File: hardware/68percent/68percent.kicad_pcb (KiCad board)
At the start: 4 copper layers, 123.8 x 142.9 mm, 119 parts, among them IC1 LD1117-3.3V-SOT223, J1 Conn_01x06, SW1 ROT_SKYLOONG_HS, SW2 Push_Button, Y1 8MHz

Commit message: pcb
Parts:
- removed LED1, LED10, LED11, LED12, LED13, LED14, LED15, LED16, LED17, LED18, LED19, LED2, LED20, LED21, LED22, LED23, LED24, LED25, LED26, LED27, LED3, LED4, LED5, LED6, LED7, LED8, LED9: MX_SK6812MINI-E, PCM_marbastlib-mx:LED_MX_6028R
- removed MACRO_A1, MACRO_B1, MACRO_C1, MACRO_D1, MACRO_E1, MACRO_F1, MACRO_G1, MACRO_H1, MACRO_I1, NUM_0, NUM_1, NUM_10, NUM_2, NUM_3, NUM_4, NUM_5, NUM_6, NUM_7, NUM_8, NUM_ADD1, NUM_DIV1, NUM_ENTER1, NUM_LOCK1, NUM_MULT1, NUM_PERIOD1, NUM_SUB1: MX_SW_HS, PCM_marbastlib-mx:SW_MX_HS_CPG151101S11_1u
- removed S1, S2, S3: MX_stab, PCM_marbastlib-mx:STAB_MX_P_2u
- removed SW1: ROT_SKYLOONG_HS, PCM_marbastlib-various:ROT_SKYLOONG_HS-Switch
- added D30: 1N4148W, PCM_Diode_SMD_AKL:D_SOD-123, B.Cu at (-145.3, 39.7)
- added D31: 1N4148W, PCM_Diode_SMD_AKL:D_SOD-123, B.Cu at (-145.3, 43.8)
- added D32: 1N4148W, PCM_Diode_SMD_AKL:D_SOD-123, B.Cu at (-145.3, 47.9)
- added D33: 1N4148W, PCM_Diode_SMD_AKL:D_SOD-123, B.Cu at (-151.3, 11.0)
- added D34: 1N4148W, PCM_Diode_SMD_AKL:D_SOD-123, B.Cu at (-151.3, 15.1)
- added D35: 1N4148W, PCM_Diode_SMD_AKL:D_SOD-123, B.Cu at (-151.3, 19.2)
- added D36: 1N4148W, PCM_Diode_SMD_AKL:D_SOD-123, B.Cu at (-151.3, 23.3)
- added D37: 1N4148W, PCM_Diode_SMD_AKL:D_SOD-123, B.Cu at (-151.3, 27.4)
- added D38: 1N4148W, PCM_Diode_SMD_AKL:D_SOD-123, B.Cu at (-151.3, 31.5)
- added D39: 1N4148W, PCM_Diode_SMD_AKL:D_SOD-123, B.Cu at (-151.3, 35.6)
- added D40: 1N4148W, PCM_Diode_SMD_AKL:D_SOD-123, B.Cu at (-151.3, 39.7)
- added D41: 1N4148W, PCM_Diode_SMD_AKL:D_SOD-123, B.Cu at (-151.3, 43.8)
- added D42: 1N4148W, PCM_Diode_SMD_AKL:D_SOD-123, B.Cu at (-151.3, 47.9)
- added D43: 1N4148W, PCM_Diode_SMD_AKL:D_SOD-123, B.Cu at (-157.2, 11.0)
- added D44: 1N4148W, PCM_Diode_SMD_AKL:D_SOD-123, B.Cu at (-157.2, 15.1)
- added D45: 1N4148W, PCM_Diode_SMD_AKL:D_SOD-123, B.Cu at (-157.2, 19.2)
- added D46: 1N4148W, PCM_Diode_SMD_AKL:D_SOD-123, B.Cu at (-157.2, 23.3)
- added D47: 1N4148W, PCM_Diode_SMD_AKL:D_SOD-123, B.Cu at (-157.2, 27.4)
- added D48: 1N4148W, PCM_Diode_SMD_AKL:D_SOD-123, B.Cu at (-157.2, 31.5)
- added D50: 1N4148W, PCM_Diode_SMD_AKL:D_SOD-123, B.Cu at (-157.2, 35.6)
- added D51: 1N4148W, PCM_Diode_SMD_AKL:D_SOD-123, B.Cu at (-157.2, 39.7)
- added D52: 1N4148W, PCM_Diode_SMD_AKL:D_SOD-123, B.Cu at (-157.2, 43.8)
- added D53: 1N4148W, PCM_Diode_SMD_AKL:D_SOD-123, B.Cu at (-157.2, 47.9)
- added D54: 1N4148W, PCM_Diode_SMD_AKL:D_SOD-123, B.Cu at (-163.1, 11.0)
- added D55: 1N4148W, PCM_Diode_SMD_AKL:D_SOD-123, B.Cu at (-163.1, 15.1)
- added D56: 1N4148W, PCM_Diode_SMD_AKL:D_SOD-123, B.Cu at (-163.1, 19.2)
- added D57: 1N4148W, PCM_Diode_SMD_AKL:D_SOD-123, B.Cu at (-163.1, 23.3)
- added D58: 1N4148W, PCM_Diode_SMD_AKL:D_SOD-123, B.Cu at (-163.1, 27.4)
- added D59: 1N4148W, PCM_Diode_SMD_AKL:D_SOD-123, B.Cu at (-163.1, 31.5)
- added D60: 1N4148W, PCM_Diode_SMD_AKL:D_SOD-123, B.Cu at (-163.1, 35.6)
- added D61: 1N4148W, PCM_Diode_SMD_AKL:D_SOD-123, B.Cu at (-163.1, 39.7)
- added D62: 1N4148W, PCM_Diode_SMD_AKL:D_SOD-123, B.Cu at (-163.1, 43.8)
- added D64: 1N4148W, PCM_Diode_SMD_AKL:D_SOD-123, B.Cu at (-163.1, 47.9)
- added D65: 1N4148W, PCM_Diode_SMD_AKL:D_SOD-123, B.Cu at (-169.0, 11.0)
- added D68: 1N4148W, PCM_Diode_SMD_AKL:D_SOD-123, B.Cu at (-169.0, 15.1)
- added D71: 1N4148W, PCM_Diode_SMD_AKL:D_SOD-123, B.Cu at (-169.0, 19.2)
- added D72: 1N4148W, PCM_Diode_SMD_AKL:D_SOD-123, B.Cu at (-169.0, 23.3)
- added D73: 1N4148W, PCM_Diode_SMD_AKL:D_SOD-123, B.Cu at (-169.0, 27.4)
- added D74: 1N4148W, PCM_Diode_SMD_AKL:D_SOD-123, B.Cu at (-169.0, 31.5)
- added D75: 1N4148W, PCM_Diode_SMD_AKL:D_SOD-123, B.Cu at (-169.0, 35.6)
- added D76: 1N4148W, PCM_Diode_SMD_AKL:D_SOD-123, B.Cu at (-169.0, 39.7)
- added KEY_'1: MX_SW_HS, PCM_marbastlib-mx:SW_MX_HS_CPG151101S11_1u, B.Cu at (-35.6, 16.5)
- added KEY_,1: MX_SW_HS, PCM_marbastlib-mx:SW_MX_HS_CPG151101S11_1u, B.Cu at (-35.6, 31.5)
- added KEY_.1: MX_SW_HS, PCM_marbastlib-mx:SW_MX_HS_CPG151101S11_1u, B.Cu at (-35.6, 46.6)
- added KEY_/1: MX_SW_HS, PCM_marbastlib-mx:SW_MX_HS_CPG151101S11_1u, B.Cu at (-35.6, 61.6)
- added KEY_0: MX_SW_HS, PCM_marbastlib-mx:SW_MX_HS_CPG151101S11_1u, B.Cu at (-18.4, 16.5)
- added KEY_1: MX_SW_HS, PCM_marbastlib-mx:SW_MX_HS_CPG151101S11_1u, B.Cu at (-18.4, 31.5)
- added KEY_2: MX_SW_HS, PCM_marbastlib-mx:SW_MX_HS_CPG151101S11_1u, B.Cu at (-18.4, 46.6)
- added KEY_3: MX_SW_HS, PCM_marbastlib-mx:SW_MX_HS_CPG151101S11_1u, B.Cu at (-18.4, 61.6)
- added KEY_4: MX_SW_HS, PCM_marbastlib-mx:SW_MX_HS_CPG151101S11_1u, B.Cu at (-18.4, 76.7)
- added KEY_5: MX_SW_HS, PCM_marbastlib-mx:SW_MX_HS_CPG151101S11_1u, B.Cu at (-18.4, 91.7)
- added KEY_6: MX_SW_HS, PCM_marbastlib-mx:SW_MX_HS_CPG151101S11_1u, B.Cu at (-18.4, 106.8)
- added KEY_7: MX_SW_HS, PCM_marbastlib-mx:SW_MX_HS_CPG151101S11_1u, B.Cu at (-18.4, 121.8)
- added KEY_8: MX_SW_HS, PCM_marbastlib-mx:SW_MX_HS_CPG151101S11_1u, B.Cu at (-18.4, 136.9)
- added KEY_9: MX_SW_HS, PCM_marbastlib-mx:SW_MX_HS_CPG151101S11_1u, B.Cu at (-18.4, 151.9)
- added KEY_;1: MX_SW_HS, PCM_marbastlib-mx:SW_MX_HS_CPG151101S11_1u, B.Cu at (-35.6, 76.7)
- added KEY_A1: MX_SW_HS, PCM_marbastlib-mx:SW_MX_HS_CPG151101S11_1u, B.Cu at (-35.6, 91.7)
- added KEY_ALT1: MX_SW_HS, PCM_marbastlib-mx:SW_MX_HS_CPG151101S11_1u, B.Cu at (-35.6, 106.8)
- added KEY_ALT2: MX_SW_HS, PCM_marbastlib-mx:SW_MX_HS_CPG151101S11_1u, B.Cu at (-35.6, 121.8)
- added KEY_B1: MX_SW_HS, PCM_marbastlib-mx:SW_MX_HS_CPG151101S11_1u, B.Cu at (-35.6, 136.9)
- added KEY_BKSP1: MX_SW_HS, PCM_marbastlib-mx:SW_MX_HS_CPG151101S11_1u, B.Cu at (-35.6, 151.9)
- added KEY_C1: MX_SW_HS, PCM_marbastlib-mx:SW_MX_HS_CPG151101S11_1u, B.Cu at (-52.7, 16.5)
- added KEY_CAPS1: MX_SW_HS, PCM_marbastlib-mx:SW_MX_HS_CPG151101S11_1u, B.Cu at (-52.7, 31.5)
- added KEY_CTRL1: MX_SW_HS, PCM_marbastlib-mx:SW_MX_HS_CPG151101S11_1u, B.Cu at (-52.7, 46.6)
- added KEY_CTRL2: MX_SW_HS, PCM_marbastlib-mx:SW_MX_HS_CPG151101S11_1u, B.Cu at (-52.7, 61.6)
- added KEY_D1: MX_SW_HS, PCM_marbastlib-mx:SW_MX_HS_CPG151101S11_1u, B.Cu at (-52.7, 76.7)
- added KEY_DARROW1: MX_SW_HS, PCM_marbastlib-mx:SW_MX_HS_CPG151101S11_1u, B.Cu at (-52.7, 91.7)
- added KEY_DARROW2: MX_SW_HS, PCM_marbastlib-mx:SW_MX_HS_CPG151101S11_1u, B.Cu at (-52.7, 106.8)
- added KEY_DEL1: MX_SW_HS, PCM_marbastlib-mx:SW_MX_HS_CPG151101S11_1u, B.Cu at (-52.7, 121.8)
- added KEY_E1: MX_SW_HS, PCM_marbastlib-mx:SW_MX_HS_CPG151101S11_1u, B.Cu at (-52.7, 136.9)
- added KEY_ENTER1: MX_SW_HS, PCM_marbastlib-mx:SW_MX_HS_CPG151101S11_1u, B.Cu at (-52.7, 151.9)
- added KEY_ESC1: MX_SW_HS, PCM_marbastlib-mx:SW_MX_HS_CPG151101S11_1u, B.Cu at (-69.9, 16.5)
- added KEY_F1: MX_SW_HS, PCM_marbastlib-mx:SW_MX_HS_CPG151101S11_1u, B.Cu at (-69.9, 31.5)
- added KEY_FN1: MX_SW_HS, PCM_marbastlib-mx:SW_MX_HS_CPG151101S11_1u, B.Cu at (-69.9, 46.6)
- added KEY_G1: MX_SW_HS, PCM_marbastlib-mx:SW_MX_HS_CPG151101S11_1u, B.Cu at (-69.9, 61.6)
- added KEY_H1: MX_SW_HS, PCM_marbastlib-mx:SW_MX_HS_CPG151101S11_1u, B.Cu at (-69.9, 76.7)
- added KEY_HOME1: MX_SW_HS, PCM_marbastlib-mx:SW_MX_HS_CPG151101S11_1u, B.Cu at (-69.9, 91.7)
- added KEY_I1: MX_SW_HS, PCM_marbastlib-mx:SW_MX_HS_CPG151101S11_1u, B.Cu at (-69.9, 106.8)
- added KEY_J1: MX_SW_HS, PCM_marbastlib-mx:SW_MX_HS_CPG151101S11_1u, B.Cu at (-69.9, 121.8)
- added KEY_K1: MX_SW_HS, PCM_marbastlib-mx:SW_MX_HS_CPG151101S11_1u, B.Cu at (-69.9, 136.9)
- added KEY_L1: MX_SW_HS, PCM_marbastlib-mx:SW_MX_HS_CPG151101S11_1u, B.Cu at (-69.9, 151.9)
- added KEY_M1: MX_SW_HS, PCM_marbastlib-mx:SW_MX_HS_CPG151101S11_1u, B.Cu at (-87.0, 16.5)
- added KEY_MINUS1: MX_SW_HS, PCM_marbastlib-mx:SW_MX_HS_CPG151101S11_1u, B.Cu at (-87.0, 31.5)
- added KEY_N1: MX_SW_HS, PCM_marbastlib-mx:SW_MX_HS_CPG151101S11_1u, B.Cu at (-87.0, 46.6)
- added KEY_O1: MX_SW_HS, PCM_marbastlib-mx:SW_MX_HS_CPG151101S11_1u, B.Cu at (-87.0, 61.6)
- added KEY_P1: MX_SW_HS, PCM_marbastlib-mx:SW_MX_HS_CPG151101S11_1u, B.Cu at (-87.0, 76.7)
- added KEY_PGDN1: MX_SW_HS, PCM_marbastlib-mx:SW_MX_HS_CPG151101S11_1u, B.Cu at (-87.0, 91.7)
- added KEY_PGUP1: MX_SW_HS, PCM_marbastlib-mx:SW_MX_HS_CPG151101S11_1u, B.Cu at (-87.0, 106.8)
- added KEY_PLUS1: MX_SW_HS, PCM_marbastlib-mx:SW_MX_HS_CPG151101S11_1u, B.Cu at (-87.0, 121.8)
- added KEY_Q1: MX_SW_HS, PCM_marbastlib-mx:SW_MX_HS_CPG151101S11_1u, B.Cu at (-87.0, 136.9)
- added KEY_R1: MX_SW_HS, PCM_marbastlib-mx:SW_MX_HS_CPG151101S11_1u, B.Cu at (-87.0, 151.9)
- added KEY_RARROW1: MX_SW_HS, PCM_marbastlib-mx:SW_MX_HS_CPG151101S11_1u, B.Cu at (-104.2, 16.5)
- added KEY_S1: MX_SW_HS, PCM_marbastlib-mx:SW_MX_HS_CPG151101S11_1u, B.Cu at (-104.2, 31.5)
- added KEY_SHIFT1: MX_SW_HS, PCM_marbastlib-mx:SW_MX_HS_CPG151101S11_1u, B.Cu at (-104.2, 46.6)
- added KEY_SHIFT2: MX_SW_HS, PCM_marbastlib-mx:SW_MX_HS_CPG151101S11_1u, B.Cu at (-104.2, 61.6)
- added KEY_SPACE1: MX_SW_HS, PCM_marbastlib-mx:SW_MX_HS_CPG151101S11_1u, B.Cu at (-104.2, 76.7)
- added KEY_T1: MX_SW_HS, PCM_marbastlib-mx:SW_MX_HS_CPG151101S11_1u, B.Cu at (-104.2, 91.7)
- added KEY_TAB1: MX_SW_HS, PCM_marbastlib-mx:SW_MX_HS_CPG151101S11_1u, B.Cu at (-104.2, 106.8)
- added KEY_U1: MX_SW_HS, PCM_marbastlib-mx:SW_MX_HS_CPG151101S11_1u, B.Cu at (-104.2, 121.8)
- added KEY_UARROW1: MX_SW_HS, PCM_marbastlib-mx:SW_MX_HS_CPG151101S11_1u, B.Cu at (-104.2, 136.9)
- added KEY_V1: MX_SW_HS, PCM_marbastlib-mx:SW_MX_HS_CPG151101S11_1u, B.Cu at (-104.2, 151.9)
- added KEY_W1: MX_SW_HS, PCM_marbastlib-mx:SW_MX_HS_CPG151101S11_1u, B.Cu at (-121.3, 16.5)
- added KEY_WIN1: MX_SW_HS, PCM_marbastlib-mx:SW_MX_HS_CPG151101S11_1u, B.Cu at (-121.3, 31.5)
- added KEY_X1: MX_SW_HS, PCM_marbastlib-mx:SW_MX_HS_CPG151101S11_1u, B.Cu at (-121.3, 46.6)
- added KEY_Y1: MX_SW_HS, PCM_marbastlib-mx:SW_MX_HS_CPG151101S11_1u, B.Cu at (-121.3, 61.6)
- added KEY_Z1: MX_SW_HS, PCM_marbastlib-mx:SW_MX_HS_CPG151101S11_1u, B.Cu at (-121.3, 76.7)
- added KEY_[1: MX_SW_HS, PCM_marbastlib-mx:SW_MX_HS_CPG151101S11_1u, B.Cu at (-121.3, 91.7)
- added KEY_\1: MX_SW_HS, PCM_marbastlib-mx:SW_MX_HS_CPG151101S11_1u, B.Cu at (-121.3, 106.8)
- added KEY_]1: MX_SW_HS, PCM_marbastlib-mx:SW_MX_HS_CPG151101S11_1u, B.Cu at (-121.3, 121.8)
- East1, North1, South1: moved to B.Cu
- moved D23 309.7 mm to (-145.3, 11.0)
- moved D21 288.8 mm to (-139.4, 43.8), turned to 180 degrees
- moved D14 283.1 mm to (-139.4, 15.1), turned to 180 degrees
- moved D20 281.8 mm to (-139.4, 39.7)
- moved D17 279.0 mm to (-139.4, 27.4)
- moved D13 278.0 mm to (-139.4, 11.0)
- moved D6 273.5 mm to (-133.5, 23.3)
- moved D19 266.2 mm to (-139.4, 35.6)
- moved D10 265.9 mm to (-133.5, 39.7), turned to 180 degrees
- moved D9 265.8 mm to (-133.5, 35.6)
- moved D16 263.4 mm to (-139.4, 23.3)
- moved D22 261.3 mm to (-139.4, 47.9)
- moved D5 255.5 mm to (-133.5, 19.2)
- moved D18 251.1 mm to (-139.4, 31.5)
- moved D8 248.4 mm to (-133.5, 31.5)
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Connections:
- D10 pad 1: /ROW2 -> /ROW1
- D11 pad 1: /ROW3 -> /ROW1
- D12 pad 1: /ROW3 -> /ROW1
- D13 pad 1: /ROW3 -> /ROW1
- D14 pad 1: /ROW3 -> /ROW1
- D15 pad 1: /ROW4 -> /ROW1
- D16 pad 1: /ROW4 -> /ROW1
- D17 pad 1: /ROW4 -> /ROW1
- D18 pad 1: /ROW5 -> /ROW2
- D19 pad 1: /ROW5 -> /ROW3
- D20 pad 1: /ROW5 -> /ROW4
- D22 pad 1: /ROW6 -> /ROW2
- D23 pad 1: /ROW6 -> /ROW2
- D25 pad 1: /ROW3 -> /ROW2
- D26 pad 1: /ROW4 -> /ROW2
- D27 pad 1: /ROW5 -> /ROW2
- D28 pad 1: /ROW6 -> /ROW2
- D29 pad 1: /ROT_SW -> /ROW2
- D7 pad 1: /ROW2 -> /ROW1
- D8 pad 1: /ROW2 -> /ROW1
- D9 pad 1: /ROW2 -> /ROW1
- U1 pad 24: /ROW6 -> unconnected-(U1-PC4-Pad24)
- U1 pad 34: unconnected-(U1-PB13-Pad34) -> /COL15
- U1 pad 35: unconnected-(U1-PB14-Pad35) -> /COL14
- U1 pad 36: unconnected-(U1-PB15-Pad36) -> /COL13
- U1 pad 37: /COL5 -> /COL12
- U1 pad 38: /COL4 -> /COL11
- U1 pad 39: /COL3 -> /COL10
- U1 pad 40: /COL2 -> /COL9
- U1 pad 41: /COL1 -> /COL8
- U1 pad 50: unconnected-(U1-PA15-Pad50) -> /COL7
- U1 pad 51: unconnected-(U1-PA10-Pad51) -> /COL6
- U1 pad 52: unconnected-(U1-PC11-Pad52) -> /COL5
- U1 pad 56: unconnected-(U1-PB4-Pad56) -> /COL4
- U1 pad 57: unconnected-(U1-PB5-Pad57) -> /COL3
- U1 pad 58: unconnected-(U1-PB6-Pad58) -> /COL2
- U1 pad 59: unconnected-(U1-PB7-Pad59) -> /COL1
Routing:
- net /COL5: track 194.0 -> 0.00 mm, vias 4 -> 0
- net /COL4: track 190.3 -> 0.00 mm, vias 9 -> 0
- net /COL2: track 163.3 -> 0.00 mm, vias 9 -> 0
- net /ROW6: track 163.0 -> 0.00 mm, vias 2 -> 0
- net /ROW5: track 153.8 -> 0.00 mm, vias 2 -> 0
- net /COL3: track 152.9 -> 0.00 mm, vias 8 -> 0
- net /UART_RX_SOUTH: track 122.1 -> 0.00 mm, vias 1 -> 0
- net /UART_TX_SOUTH: track 119.9 -> 0.00 mm, vias 2 -> 0
- net /UART_TX_EAST: track 112.8 -> 0.00 mm, vias 1 -> 0
- net /ROW3: track 111.9 -> 0.00 mm, vias 2 -> 0
- net /UART_RX_EAST: track 111.0 -> 0.00 mm, vias 1 -> 0
- net /ROW2: track 102.4 -> 0.00 mm, vias 4 -> 0
- net /COL1: track 95.3 -> 0.00 mm, vias 5 -> 0
- net /ROW4: track 87.6 -> 0.00 mm, vias 2 -> 0
- net /ROW1: track 86.9 -> 0.00 mm, vias 3 -> 0
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- removed copper zone on In2.Cu, net +3.3V
- removed copper zone on In2.Cu, net +5V
- removed copper zone on In1.Cu, net AGND
- removed copper zone on In1.Cu, net GND
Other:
- board outline removed
- board text removed: "${REFERENCE}"
- board text removed: "5VD"
- board text removed: "ARHKEIA"
- board text removed: "Team SKBD Numpad"

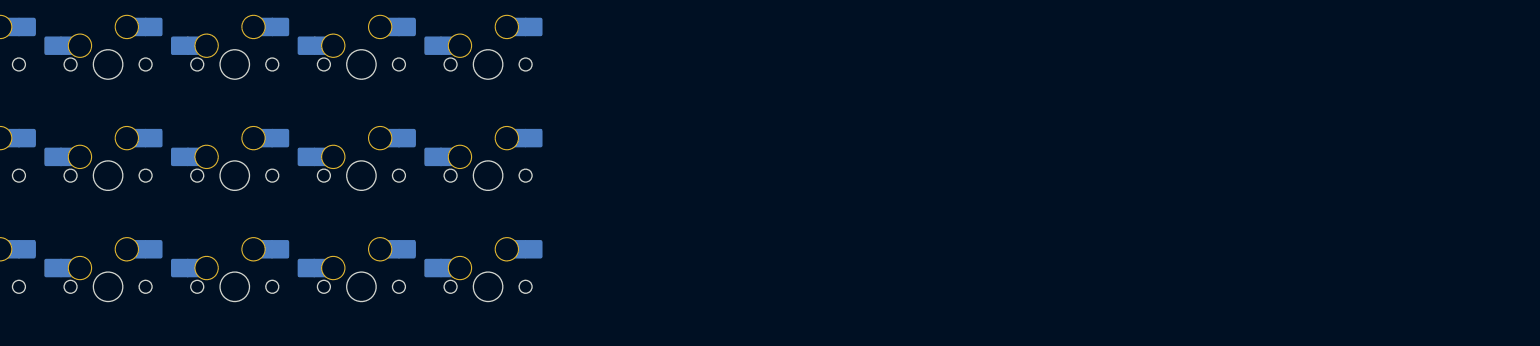
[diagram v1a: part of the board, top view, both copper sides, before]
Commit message: PCB start for keyboard
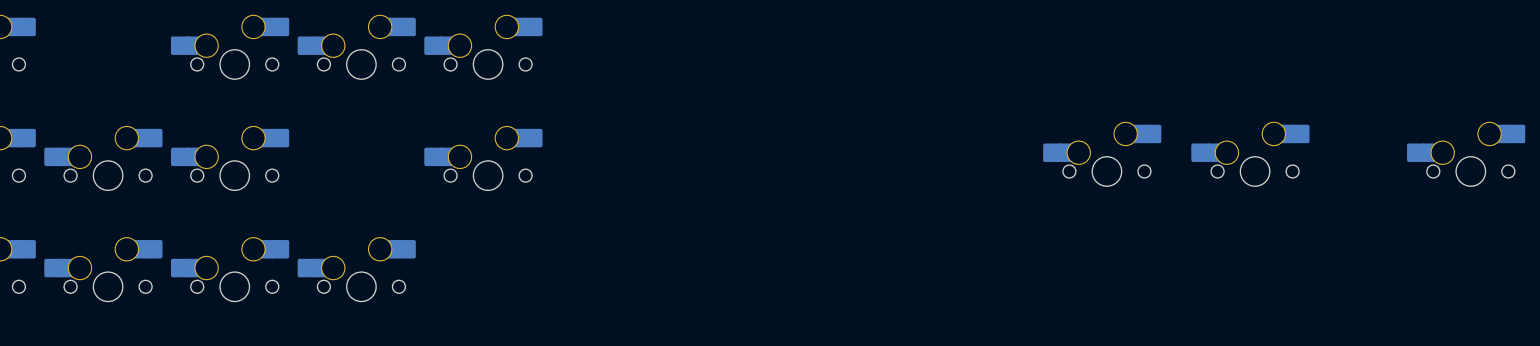
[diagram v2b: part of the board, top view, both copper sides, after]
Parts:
- moved KEY_ESC1 136.0 mm to (65.3, 31.0)
- moved KEY_2 134.0 mm to (114.6, 31.0)
- moved KEY_,1 121.0 mm to (85.4, 31.0)
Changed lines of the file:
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@@
 	(footprint "PCM_marbastlib-mx:SW_MX_HS_CPG151101S11_1u"
 		(layer "B.Cu")
-		(at -18.438824 46.567 180)
+		(at 114.6175 30.95625 180)
 		(descr "Footprint for Cherry MX style switches with Kailh hotswap socket")
 		(property "Reference" "KEY_2"
@@
 	(footprint "PCM_marbastlib-mx:SW_MX_HS_CPG151101S11_1u"
 		(layer "B.Cu")
-		(at -69.888824 16.467 180)
+		(at 65.3475 30.95625 180)
 		(descr "Footprint for Cherry MX style switches with Kailh hotswap socket")
 		(property "Reference" "KEY_ESC1"
@@
 	(footprint "PCM_marbastlib-mx:SW_MX_HS_CPG151101S11_1u"
 		(layer "B.Cu")
-		(at -35.588824 31.517 180)
+		(at 85.4075 30.95625 180)
 		(descr "Footprint for Cherry MX style switches with Kailh hotswap socket")
 		(property "Reference" "KEY_,1"

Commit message: more pcb work
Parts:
- moved KEY_9 274.7 mm to (229.5, 33.5)
- moved KEY_0 267.5 mm to (248.5, 33.5)
- moved KEY_8 251.1 mm to (210.4, 33.5)
- moved KEY_7 227.6 mm to (191.4, 33.5)
- moved KEY_6 204.3 mm to (172.3, 33.5)
- moved KEY_5 181.3 mm to (153.3, 33.5)
- moved KEY_4 154.2 mm to (129.6, 33.5)
- moved KEY_,1 144.4 mm to (-54.6, -4.60)
- moved KEY_3 125.9 mm to (104.2, 33.5)
- moved KEY_1 70.9 mm to (52.4, 33.5)
- moved KEY_ESC1 37.2 mm to (28.3, 33.5)
- moved KEY_2 35.8 mm to (78.9, 33.5)
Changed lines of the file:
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@@
 	(footprint "PCM_marbastlib-mx:SW_MX_HS_CPG151101S11_1u"
 		(layer "B.Cu")
-		(at -18.438824 31.517 180)
+		(at 52.3875 33.49625 180)
 		(descr "Footprint for Cherry MX style switches with Kailh hotswap socket")
 		(property "Reference" "KEY_1"
@@
 	(footprint "PCM_marbastlib-mx:SW_MX_HS_CPG151101S11_1u"
 		(layer "B.Cu")
-		(at -18.438824 16.467 180)
+		(at 248.5225 33.49625 180)
 		(descr "Footprint for Cherry MX style switches with Kailh hotswap socket")
 		(property "Reference" "KEY_0"
@@
 	(footprint "PCM_marbastlib-mx:SW_MX_HS_CPG151101S11_1u"
 		(layer "B.Cu")
-		(at 114.6175 30.95625 180)
+		(at 78.8895 33.49625 180)
 		(descr "Footprint for Cherry MX style switches with Kailh hotswap socket")
 		(property "Reference" "KEY_2"
@@
 	(footprint "PCM_marbastlib-mx:SW_MX_HS_CPG151101S11_1u"
 		(layer "B.Cu")
-		(at -18.438824 136.867 180)
+		(at 210.4225 33.49625 180)
 		(descr "Footprint for Cherry MX style switches with Kailh hotswap socket")
 		(property "Reference" "KEY_8"
@@
 	(footprint "PCM_marbastlib-mx:SW_MX_HS_CPG151101S11_1u"
 		(layer "B.Cu")
-		(at -18.438824 106.767 180)
+		(at 172.3225 33.49625 180)
 		(descr "Footprint for Cherry MX style switches with Kailh hotswap socket")
 		(property "Reference" "KEY_6"
@@
 	(footprint "PCM_marbastlib-mx:SW_MX_HS_CPG151101S11_1u"
 		(layer "B.Cu")
-		(at 65.3475 30.95625 180)
+		(at 28.2575 33.49625 180)
 		(descr "Footprint for Cherry MX style switches with Kailh hotswap socket")
 		(property "Reference" "KEY_ESC1"
@@
 	(footprint "PCM_marbastlib-mx:SW_MX_HS_CPG151101S11_1u"
 		(layer "B.Cu")
-		(at -18.438824 61.617 180)
+		(at 104.2435 33.49625 180)
 		(descr "Footprint for Cherry MX style switches with Kailh hotswap socket")
 		(property "Reference" "KEY_3"
@@
 	(footprint "PCM_marbastlib-mx:SW_MX_HS_CPG151101S11_1u"
 		(layer "B.Cu")
-		(at -18.438824 76.667 180)
+		(at 129.5975 33.49625 180)
 		(descr "Footprint for Cherry MX style switches with Kailh hotswap socket")
 		(property "Reference" "KEY_4"
@@
 	(footprint "PCM_marbastlib-mx:SW_MX_HS_CPG151101S11_1u"
 		(layer "B.Cu")
-		(at 85.4075 30.95625 180)
+		(at -54.5525 -4.60375 180)
 		(descr "Footprint for Cherry MX style switches with Kailh hotswap socket")
 		(property "Reference" "KEY_,1"
@@
 	(footprint "PCM_marbastlib-mx:SW_MX_HS_CPG151101S11_1u"
 		(layer "B.Cu")
-		(at -18.438824 121.817 180)
+		(at 191.3725 33.49625 180)
 		(descr "Footprint for Cherry MX style switches with Kailh hotswap socket")
 		(property "Reference" "KEY_7"
@@
 	(footprint "PCM_marbastlib-mx:SW_MX_HS_CPG151101S11_1u"
 		(layer "B.Cu")
-		(at -18.438824 91.717 180)
+		(at 153.2725 33.49625 180)
 		(descr "Footprint for Cherry MX style switches with Kailh hotswap socket")
 		(property "Reference" "KEY_5"
@@
 	(footprint "PCM_marbastlib-mx:SW_MX_HS_CPG151101S11_1u"
 		(layer "B.Cu")
-		(at -18.438824 151.917 180)
+		(at 229.4725 33.49625 180)
 		(descr "Footprint for Cherry MX style switches with Kailh hotswap socket")
 		(property "Reference" "KEY_9"

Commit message: keyboard updates
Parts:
- moved KEY_HOME1 388.7 mm to (314.0, 31.0)
- moved KEY_PLUS1 347.6 mm to (248.5, 31.0)
- moved KEY_BKSP1 343.6 mm to (286.1, 31.0)
- moved KEY_MINUS1 316.5 mm to (229.5, 31.0)
- moved KEY_U1 285.1 mm to (171.8, 50.0)
- moved KEY_Y1 274.3 mm to (152.7, 50.0)
- moved KEY_T1 241.5 mm to (133.7, 50.0)
- moved KEY_R1 225.9 mm to (114.6, 50.0)
- moved KEY_W1 200.7 mm to (76.5, 50.0)
- moved KEY_E1 171.9 mm to (95.6, 50.0)
- moved KEY_Q1 168.6 mm to (57.5, 50.0)
- moved KEY_TAB1 145.7 mm to (30.0, 50.0)
- moved KEY_8 38.2 mm to (172.3, 31.0)
- moved KEY_5 38.2 mm to (115.2, 31.0)
- moved KEY_0 38.2 mm to (210.4, 31.0)
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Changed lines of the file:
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@@
 	(footprint "PCM_marbastlib-mx:SW_MX_HS_CPG151101S11_1u"
 		(layer "B.Cu")
-		(at 52.3875 33.49625 180)
+		(at 38.9725 30.95625 180)
 		(descr "Footprint for Cherry MX style switches with Kailh hotswap socket")
 		(property "Reference" "KEY_1"
@@
 	(footprint "PCM_marbastlib-mx:SW_MX_HS_CPG151101S11_1u"
 		(layer "B.Cu")
-		(at -69.888824 91.717 180)
+		(at 314.0075 30.95625 180)
 		(descr "Footprint for Cherry MX style switches with Kailh hotswap socket")
 		(property "Reference" "KEY_HOME1"
@@
 	(footprint "PCM_marbastlib-mx:SW_MX_HS_CPG151101S11_1u"
 		(layer "B.Cu")
-		(at 248.5225 33.49625 180)
+		(at 210.4225 30.95625 180)
 		(descr "Footprint for Cherry MX style switches with Kailh hotswap socket")
 		(property "Reference" "KEY_0"
@@
 	(footprint "PCM_marbastlib-mx:SW_MX_HS_CPG151101S11_1u"
 		(layer "B.Cu")
-		(at -104.188824 121.817 180)
+		(at 171.7675 50.00625 180)
 		(descr "Footprint for Cherry MX style switches with Kailh hotswap socket")
 		(property "Reference" "KEY_U1"
@@
 	(footprint "PCM_marbastlib-mx:SW_MX_HS_CPG151101S11_1u"
 		(layer "B.Cu")
-		(at 78.8895 33.49625 180)
+		(at 58.0225 30.95625 180)
 		(descr "Footprint for Cherry MX style switches with Kailh hotswap socket")
 		(property "Reference" "KEY_2"
@@
 	(footprint "PCM_marbastlib-mx:SW_MX_HS_CPG151101S11_1u"
 		(layer "B.Cu")
-		(at 210.4225 33.49625 180)
+		(at 172.3225 30.95625 180)
 		(descr "Footprint for Cherry MX style switches with Kailh hotswap socket")
 		(property "Reference" "KEY_8"
@@
 	(footprint "PCM_marbastlib-mx:SW_MX_HS_CPG151101S11_1u"
 		(layer "B.Cu")
-		(at 172.3225 33.49625 180)
+		(at 134.2225 30.95625 180)
 		(descr "Footprint for Cherry MX style switches with Kailh hotswap socket")
 		(property "Reference" "KEY_6"
@@
 	(footprint "PCM_marbastlib-mx:SW_MX_HS_CPG151101S11_1u"
 		(layer "B.Cu")
-		(at 28.2575 33.49625 180)
+		(at 19.9 30.95625 180)
 		(descr "Footprint for Cherry MX style switches with Kailh hotswap socket")
 		(property "Reference" "KEY_ESC1"
@@
 	(footprint "PCM_marbastlib-mx:SW_MX_HS_CPG151101S11_1u"
 		(layer "B.Cu")
-		(at 104.2435 33.49625 180)
+		(at 77.0725 30.95625 180)
 		(descr "Footprint for Cherry MX style switches with Kailh hotswap socket")
 		(property "Reference" "KEY_3"
@@
 	(footprint "PCM_marbastlib-mx:SW_MX_HS_CPG151101S11_1u"
 		(layer "B.Cu")
-		(at -104.188824 91.717 180)
+		(at 133.6675 50.00625 180)
 		(descr "Footprint for Cherry MX style switches with Kailh hotswap socket")
 		(property "Reference" "KEY_T1"
@@
 	(footprint "PCM_marbastlib-mx:SW_MX_HS_CPG151101S11_1u"
 		(layer "B.Cu")
-		(at 129.5975 33.49625 180)
+		(at 96.1225 30.95625 180)
 		(descr "Footprint for Cherry MX style switches with Kailh hotswap socket")
 		(property "Reference" "KEY_4"
@@
 	(footprint "PCM_marbastlib-mx:SW_MX_HS_CPG151101S11_1u"
 		(layer "B.Cu")
-		(at -87.038824 136.867 180)
+		(at 57.4675 50.00625 180)
 		(descr "Footprint for Cherry MX style switches with Kailh hotswap socket")
 		(property "Reference" "KEY_Q1"
@@
 	(footprint "PCM_marbastlib-mx:SW_MX_HS_CPG151101S11_1u"
 		(layer "B.Cu")
-		(at -87.038824 151.917 180)
+		(at 114.6175 50.00625 180)
 		(descr "Footprint for Cherry MX style switches with Kailh hotswap socket")
 		(property "Reference" "KEY_R1"
@@
 	(footprint "PCM_marbastlib-mx:SW_MX_HS_CPG151101S11_1u"
 		(layer "B.Cu")
-		(at -104.188824 106.767 180)
+		(at 30 50.00625 180)
 		(descr "Footprint for Cherry MX style switches with Kailh hotswap socket")
 		(property "Reference" "KEY_TAB1"
@@
 	(footprint "PCM_marbastlib-mx:SW_MX_HS_CPG151101S11_1u"
 		(layer "B.Cu")
-		(at -52.738824 136.867 180)
+		(at 95.5675 50.00625 180)
 		(descr "Footprint for Cherry MX style switches with Kailh hotswap socket")
 		(property "Reference" "KEY_E1"
@@
 	(footprint "PCM_marbastlib-mx:SW_MX_HS_CPG151101S11_1u"
 		(layer "B.Cu")
-		(at -35.588824 151.917 180)
+		(at 286.0675 30.95625 180)
 		(descr "Footprint for Cherry MX style switches with Kailh hotswap socket")
 		(property "Reference" "KEY_BKSP1"
@@
 	(footprint "PCM_marbastlib-mx:SW_MX_HS_CPG151101S11_1u"
 		(layer "B.Cu")
-		(at -87.038824 31.517 180)
+		(at 229.4725 30.95625 180)
 		(descr "Footprint for Cherry MX style switches with Kailh hotswap socket")
 		(property "Reference" "KEY_MINUS1"
@@
 	(footprint "PCM_marbastlib-mx:SW_MX_HS_CPG151101S11_1u"
 		(layer "B.Cu")
-		(at -121.338824 61.617 180)
+		(at 152.7175 50.00625 180)
 		(descr "Footprint for Cherry MX style switches with Kailh hotswap socket")
 		(property "Reference" "KEY_Y1"
@@
 	(footprint "PCM_marbastlib-mx:SW_MX_HS_CPG151101S11_1u"
 		(layer "B.Cu")
-		(at -87.038824 121.817 180)
+		(at 248.5 30.95625 180)
 		(descr "Footprint for Cherry MX style switches with Kailh hotswap socket")
 		(property "Reference" "KEY_PLUS1"
@@
 	(footprint "PCM_marbastlib-mx:SW_MX_HS_CPG151101S11_1u"
 		(layer "B.Cu")
-		(at 191.3725 33.49625 180)
+		(at 153.2725 30.95625 180)
 		(descr "Footprint for Cherry MX style switches with Kailh hotswap socket")
 		(property "Reference" "KEY_7"
@@
 	(footprint "PCM_marbastlib-mx:SW_MX_HS_CPG151101S11_1u"
 		(layer "B.Cu")
-		(at 153.2725 33.49625 180)
+		(at 115.1725 30.95625 180)
 		(descr "Footprint for Cherry MX style switches with Kailh hotswap socket")
 		(property "Reference" "KEY_5"
@@
 	(footprint "PCM_marbastlib-mx:SW_MX_HS_CPG151101S11_1u"
 		(layer "B.Cu")
-		(at 229.4725 33.49625 180)
+		(at 191.3725 30.95625 180)
 		(descr "Footprint for Cherry MX style switches with Kailh hotswap socket")
 		(property "Reference" "KEY_9"
@@
 	(footprint "PCM_marbastlib-mx:SW_MX_HS_CPG151101S11_1u"
 		(layer "B.Cu")
-		(at -121.338824 16.467 180)
+		(at 76.5175 50.00625 180)
 		(descr "Footprint for Cherry MX style switches with Kailh hotswap socket")
 		(property "Reference" "KEY_W1"

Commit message: chicken butt
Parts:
- added BackspStab1: MX_stab, PCM_marbastlib-mx:STAB_MX_P_2u, F.Cu at (295.3, 35.9)
- added EnterStab1: MX_stab, PCM_marbastlib-mx:STAB_MX_P_2.25u, F.Cu at (152.4, -47.6)
- added LeftStab1: MX_stab, PCM_marbastlib-mx:STAB_MX_P_2.25u, F.Cu at (33.3, -19.1)
- added RightStab1: MX_stab, PCM_marbastlib-mx:STAB_MX_P_2u, F.Cu at (169.1, -13.0)
- added Space_Stab1: MX_stab, PCM_marbastlib-mx:STAB_MX_P_6.25u, F.Cu at (95.2, 4.76)
- moved KEY_6 18.8 mm to (152.4, 35.9)
- moved KEY_8 18.8 mm to (190.5, 35.9)
- moved KEY_9 18.8 mm to (209.6, 35.9)
- moved KEY_MINUS1 18.8 mm to (247.7, 35.9)
- moved KEY_PLUS1 18.8 mm to (266.7, 35.9)
- moved KEY_1 18.8 mm to (57.1, 35.9)
- moved KEY_2 18.8 mm to (76.2, 35.9)
- moved KEY_ESC1 18.8 mm to (38.1, 35.9)
- moved KEY_3 18.8 mm to (95.2, 35.9)
- moved KEY_4 18.8 mm to (114.3, 35.9)
- moved KEY_5 18.8 mm to (133.3, 35.9)
- moved KEY_0 18.8 mm to (228.6, 35.9)
- moved KEY_7 18.8 mm to (171.4, 35.9)
- moved KEY_TAB1 13.8 mm to (42.9, 54.9)
- moved KEY_HOME1 11.0 mm to (323.9, 35.9)
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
